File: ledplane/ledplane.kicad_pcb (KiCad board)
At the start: 2 copper layers, 100 x 100 mm, 41 parts

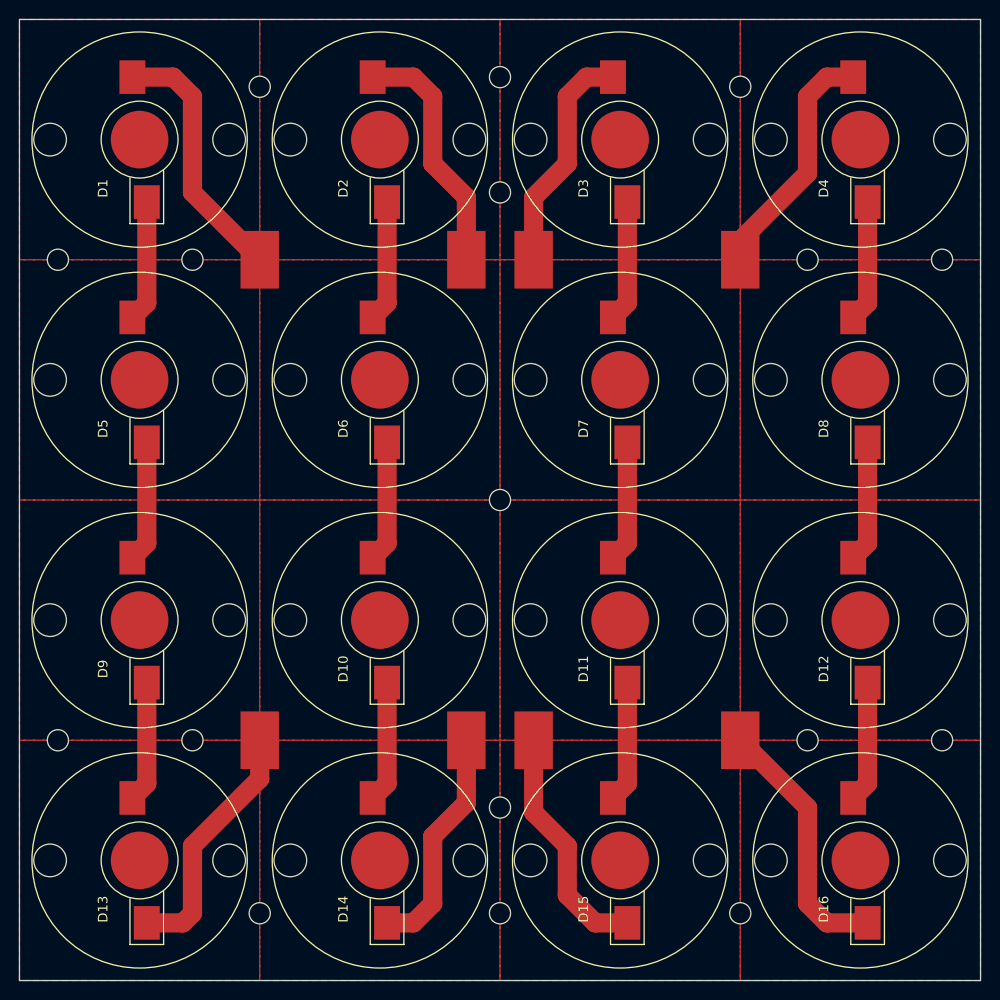
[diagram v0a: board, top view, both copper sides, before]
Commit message: Update LED plane to be all in series
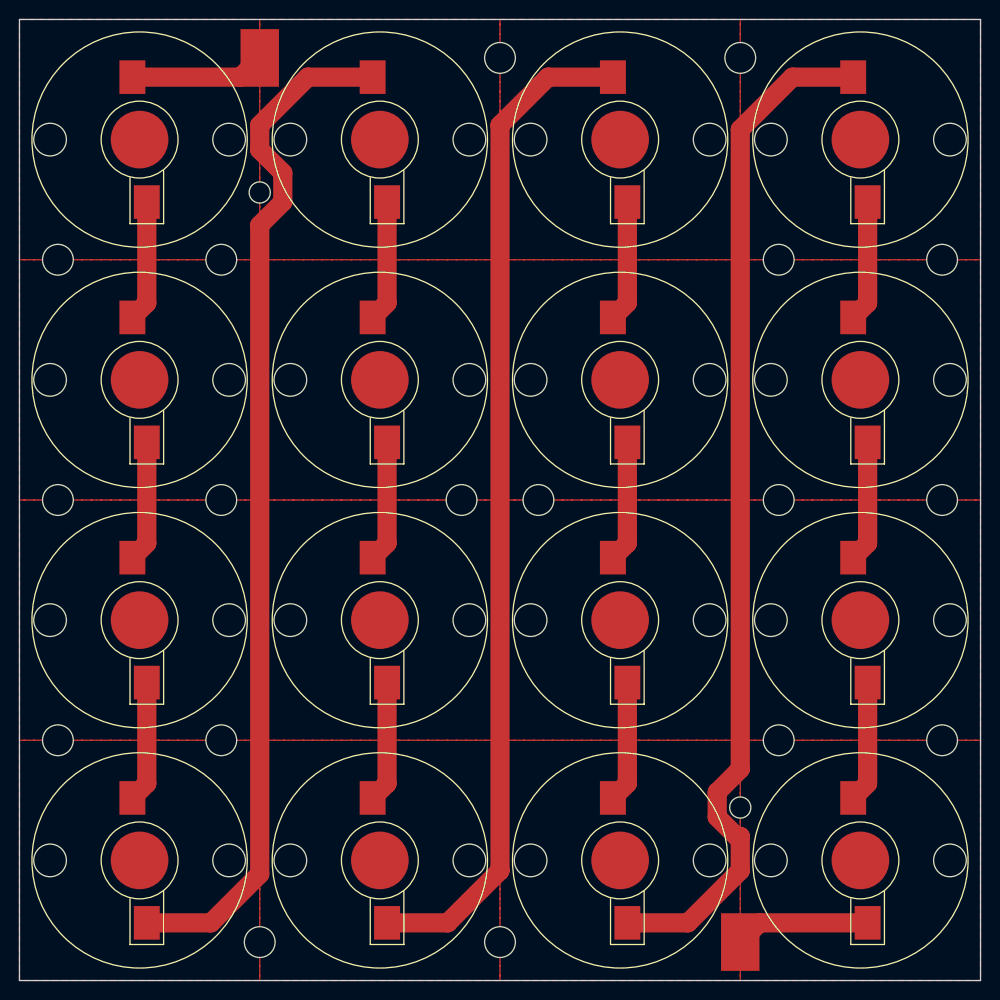
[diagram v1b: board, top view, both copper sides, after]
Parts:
- removed the H10 at (50.0, 18.0)
- removed the H6 at (25.0, 93.0)
- removed the H7 at (50.0, 6.00)
- removed the H9 at (50.0, 93.0)
- removed the TP2 at (46.5, 25.0)
- removed TP3, TP4, TP5, TP6, TP7: TestPoint, misc:SolderWirePad_1x01_SMD_4x6mm
- added H12: MountingHole, MountingHole:MountingHole_3.2mm_M3, F.Cu at (4.00, 50.0)
- added H14: MountingHole, MountingHole:MountingHole_3.2mm_M3, F.Cu at (50.0, 4.00)
- added H15: MountingHole, MountingHole:MountingHole_3.2mm_M3, F.Cu at (25.0, 96.0)
- added H17: MountingHole, MountingHole:MountingHole_3.2mm_M3, F.Cu at (79.0, 50.0)
- added H18: MountingHole, MountingHole:MountingHole_3.2mm_M3, F.Cu at (75.0, 4.00)
- added H19: MountingHole, MountingHole:MountingHole_3.2mm_M3, F.Cu at (50.0, 96.0)
- added H20: MountingHole, MountingHole:MountingHole_3.2mm_M3, F.Cu at (54.0, 50.0)
- H10: renamed from H4; footprint MountingHole:MountingHole_2.2mm_M2 -> MountingHole:MountingHole_3.2mm_M3
- H11: renamed from H12; footprint MountingHole:MountingHole_2.2mm_M2 -> MountingHole:MountingHole_3.2mm_M3
- H13, H16: footprint MountingHole:MountingHole_2.2mm_M2 -> MountingHole:MountingHole_3.2mm_M3
- H3: renamed from H1; footprint MountingHole:MountingHole_2.2mm_M2 -> MountingHole:MountingHole_3.2mm_M3
- H4: renamed from H14; footprint MountingHole:MountingHole_2.2mm_M2 -> MountingHole:MountingHole_3.2mm_M3
- H5: renamed from H2; footprint MountingHole:MountingHole_2.2mm_M2 -> MountingHole:MountingHole_3.2mm_M3
- H6: renamed from H11; footprint MountingHole:MountingHole_2.2mm_M2 -> MountingHole:MountingHole_3.2mm_M3
- H7: renamed from H15; footprint MountingHole:MountingHole_2.2mm_M2 -> MountingHole:MountingHole_3.2mm_M3
- H8: renamed from H5; footprint MountingHole:MountingHole_2.2mm_M2 -> MountingHole:MountingHole_3.2mm_M3
- H9: renamed from H8; footprint MountingHole:MountingHole_2.2mm_M2 -> MountingHole:MountingHole_3.2mm_M3
- moved H16 69.0 mm to (21.0, 50.0), turned to 0 degrees
- moved H13 56.0 mm to (96.0, 50.0), turned to 0 degrees
- moved TP1 21.0 mm to (25.0, 4.00)
- moved TP2 21.0 mm to (75.0, 96.0)
- moved H1 11.0 mm to (25.0, 18.0)
- moved H2 11.0 mm to (75.0, 82.0)
- moved H9 4.00 mm to (46.0, 50.0)
- moved H10 3.00 mm to (79.0, 25.0)
- moved H11 3.00 mm to (21.0, 75.0)
- moved H4 3.00 mm to (79.0, 75.0)
- moved H5 3.00 mm to (21.0, 25.0)
- renumbered D7 to D10, D15 to D12, D4 to D13, D8 to D14, D12 to D15, D5 to D2, D9 to D3, D13 to D4, D2 to D5, D10 to D7, D14 to D8, D3 to D9, H3 to H1, H17 to H2, TP8 to TP2
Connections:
- net Net-(D1-A) renamed VCC
- net Net-(D16-K) renamed GND
- D12 pad 1: Net-(D15-K) (its old number) -> Net-(D12-K)
- D13 pad 2: Net-(D4-A) -> Net-(D12-K)
- D4 pad 1: Net-(D13-K) (its old number) -> Net-(D4-K)
- D5 pad 2: Net-(D2-A) -> Net-(D4-K)
- D8 pad 1: Net-(D14-K) (its old number) -> Net-(D8-K)
- D9 pad 2: Net-(D3-A) -> Net-(D8-K)
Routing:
- net Net-(D4-K): track 0.00 -> 107.6 mm
- net Net-(D12-K): track 0.00 -> 107.3 mm
- net Net-(D8-K): track 0.00 -> 105.4 mm
- net Net-(D13-K) (its old number): track 26.1 -> 0.00 mm
- net Net-(D2-A): track 25.5 -> 0.00 mm
- net Net-(D4-A): track 25.5 -> 0.00 mm
- net Net-(D15-K) (its old number): track 25.0 -> 0.00 mm
- net Net-(D3-A): track 24.0 -> 0.00 mm
- net Net-(D14-K) (its old number): track 24.0 -> 0.00 mm
- net GND: track 27.0 -> 14.1 mm
- net VCC: track 27.0 -> 14.1 mm
